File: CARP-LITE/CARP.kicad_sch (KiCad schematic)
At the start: 105 parts, among them J1 USB_C_Receptacle_USB2.0_14P, J10 PYRO_2, J2 SPI1+3V3, J3 I2C1+3V3, J4 2S XT30, J5 UART+5V+I2C1, J6 PYRO_1, J8 PWM1+6V, J9 PWM2+6V, Q1 Q_NMOS, Q2 Q_NMOS, Q4 Q_NMOS, SW1 SW_Push, SW2 SW_Push, U1 W25Q128JVSIMTR (16MB), U2 W25Q32RVXHJQ (2MB), U3 3V3 LDO, U4 RP2350_60QFN, U5 LSM6DSO, U6 BMP390, U7 5V LDO, U8 6V LDO, Y1 ABM8-272-T3

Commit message: fp changes
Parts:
- removed R23: 100, PCM_Resistor_SMD_AKL:R_0603_1608Metric, symbol Device:R
- added R35: 100, Resistor_SMD:R_0603_1608Metric, symbol Device:R
- R1, R11, R14, R15, R16, R17, R18, R2, R3, R6, R7, R9: footprint PCM_Resistor_SMD_AKL:R_0603_1608Metric -> Resistor_SMD:R_0603_1608Metric
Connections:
- net GPIO21: now also R35.1
- net at C27.2, Q2.G, R25.1: now also R35.2
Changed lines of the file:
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@@
 			)
 		)
-		(property "Footprint" "PCM_Resistor_SMD_AKL:R_0603_1608Metric"
+		(property "Footprint" "Resistor_SMD:R_0603_1608Metric"
 			(at 67.31 269.748 90)
 			(hide yes)
@@
 	)
 	(symbol
+		(lib_id "Device:R")
+		(at 328.93 237.49 90)
+		(unit 1)
+		(body_style 1)
+		(exclude_from_sim no)
+		(in_bom yes)
+		(on_board yes)
+		(in_pos_files yes)
+		(dnp no)
+		(property "Reference" "R35"
+			(at 326.644 235.204 90)
+			(show_name no)
+			(do_not_autoplace no)
+			(effects
+				(font
+					(size 1.27 1.27)
+				)
+				(justify right)
+			)
+		)
+		(property "Value" "100"
+			(at 326.898 237.49 90)
+			(show_name no)
+			(do_not_autoplace no)
+			(effects
+				(font
+					(size 1.27 1.27)
+				)
+				(justify right)
+			)
+		)
+		(property "Footprint" "Resistor_SMD:R_0603_1608Metric"
+			(at 328.93 239.268 90)
+			(hide yes)
+			(show_name no)
+			(do_not_autoplace no)
+			(effects
+				(font
+					(size 1.27 1.27)
+				)
+			)
+		)
+		(property "Datasheet" ""
+			(at 328.93 237.49 0)
+			(hide yes)
+			(show_name no)
+			(do_not_autoplace no)
+			(effects
+				(font
+					(size 1.27 1.27)
+				)
+			)
+		)
+		(property "Description" ""
+			(at 328.93 237.49 0)
+			(show_name no)
+			(do_not_autoplace no)
+			(effects
+				(font
+					(size 1.27 1.27)
+				)
+			)
+		)
+		(pin "1"
+		)
+		(pin "2"
+		)
+		(instances
+			(project "CARP"
+				(path "/94683f5c-9cd9-448e-be96-9792537b5cb8"
+					(reference "R35")
+					(unit 1)
+				)
+			)
+		)
+	)
+	(symbol
 		(lib_id "power:GND")
 		(at 351.79 194.31 0)
@@
 			)
 		)
-		(property "Footprint" "PCM_Resistor_SMD_AKL:R_0603_1608Metric"
+		(property "Footprint" "Resistor_SMD:R_0603_1608Metric"
 			(at 240.03 125.222 90)
 			(hide yes)
@@
 			)
 		)
-		(property "Footprint" "PCM_Resistor_SMD_AKL:R_0603_1608Metric"
+		(property "Footprint" "Resistor_SMD:R_0603_1608Metric"
 			(at 250.825 83.312 90)
 			(hide yes)
@@
 	)
 	(symbol
-		(lib_id "Device:R")
-		(at 328.93 237.49 90)
-		(unit 1)
-		(body_style 1)
-		(exclude_from_sim no)
-		(in_bom yes)
-		(on_board yes)
-		(in_pos_files yes)
-		(dnp no)
-		(property "Reference" "R23"
-			(at 326.644 235.204 90)
-			(show_name no)
-			(do_not_autoplace no)
-			(effects
-				(font
-					(size 1.27 1.27)
-				)
-				(justify right)
-			)
-		)
-		(property "Value" "100"
-			(at 326.898 237.49 90)
-			(show_name no)
-			(do_not_autoplace no)
-			(effects
-				(font
-					(size 1.27 1.27)
-				)
-				(justify right)
-			)
-		)
-		(property "Footprint" "PCM_Resistor_SMD_AKL:R_0603_1608Metric"
-			(at 328.93 239.268 90)
-			(hide yes)
-			(show_name no)
-			(do_not_autoplace no)
-			(effects
-				(font
-					(size 1.27 1.27)
-				)
-			)
-		)
-		(property "Datasheet" ""
-			(at 328.93 237.49 0)
-			(hide yes)
-			(show_name no)
-			(do_not_autoplace no)
-			(effects
-				(font
-					(size 1.27 1.27)
-				)
-			)
-		)
-		(property "Description" ""
-			(at 328.93 237.49 0)
-			(show_name no)
-			(do_not_autoplace no)
-			(effects
-				(font
-					(size 1.27 1.27)
-				)
-			)
-		)
-		(pin "1"
-		)
-		(pin "2"
-		)
-		(instances
-			(project "CARP"
-				(path "/94683f5c-9cd9-448e-be96-9792537b5cb8"
-					(reference "R23")
-					(unit 1)
-				)
-			)
-		)
-	)
-	(symbol
 		(lib_id "Device:C")
 		(at 214.63 69.85 0)
@@
 			)
 		)
-		(property "Footprint" "PCM_Resistor_SMD_AKL:R_0603_1608Metric"
+		(property "Footprint" "Resistor_SMD:R_0603_1608Metric"
 			(at 69.342 91.44 90)
 			(hide yes)
@@
 			)
 		)
-		(property "Footprint" "PCM_Resistor_SMD_AKL:R_0603_1608Metric"
+		(property "Footprint" "Resistor_SMD:R_0603_1608Metric"
 			(at 137.922 151.13 90)
 			(hide yes)
@@
 			)
 		)
-		(property "Footprint" "PCM_Resistor_SMD_AKL:R_0603_1608Metric"
+		(property "Footprint" "Resistor_SMD:R_0603_1608Metric"
 			(at 105.918 96.52 90)
 			(hide yes)
@@
 			)
 		)
-		(property "Footprint" "PCM_Resistor_SMD_AKL:R_0603_1608Metric"
+		(property "Footprint" "Resistor_SMD:R_0603_1608Metric"
 			(at 121.92 168.148 90)
 			(hide yes)
@@
 			)
 		)
-		(property "Footprint" "PCM_Resistor_SMD_AKL:R_0603_1608Metric"
+		(property "Footprint" "Resistor_SMD:R_0603_1608Metric"
 			(at 70.612 273.05 90)
 			(hide yes)
@@
 			)
 		)
-		(property "Footprint" "PCM_Resistor_SMD_AKL:R_0603_1608Metric"
+		(property "Footprint" "Resistor_SMD:R_0603_1608Metric"
 			(at 105.918 106.68 90)
 			(hide yes)
@@
 			)
 		)
-		(property "Footprint" "PCM_Resistor_SMD_AKL:R_0603_1608Metric"
+		(property "Footprint" "Resistor_SMD:R_0603_1608Metric"
 			(at 31.75 168.148 90)
 			(hide yes)
@@
 			)
 		)
-		(property "Footprint" "PCM_Resistor_SMD_AKL:R_0603_1608Metric"
+		(property "Footprint" "Resistor_SMD:R_0603_1608Metric"
 			(at 31.75 159.258 90)
 			(hide yes)
@@
 			)
 		)
-		(property "Footprint" "PCM_Resistor_SMD_AKL:R_0603_1608Metric"
+		(property "Footprint" "Resistor_SMD:R_0603_1608Metric"
 			(at 50.292 151.13 90)
 			(hide yes)

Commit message: more fp changes
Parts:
- removed Q1, Q2, Q4: Q_NMOS, symbol Device:Q_NMOS
- added Q5, Q6, Q7: SQ2318CES, Package_TO_SOT_SMD:SOT-23, symbol Transistor_FET_Other:Q_NMOS_Depletion_GSD
- D2: footprint (none) -> LED_SMD:LED_0805_2012Metric
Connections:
- net GND: now also Q5.2 (S), Q6.2 (S), Q7.2 (S)
- net at R14.1, R15.2: now also Q7.1 (G)
- net at C27.2, R25.1, R35.2: now also Q5.1 (G)
- net at J10.2 (Pin_2), R32.2: now also Q6.3 (D)
- net at C33.2, R31.2, R33.1: now also Q6.1 (G)
- net at J6.2 (Pin_2), R24.2: now also Q5.3 (D)
- net at BZ1.2 (-), D5.2 (A): now also Q7.3 (D)

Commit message: siup
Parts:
- BZ1: footprint (none) -> Buzzer_Beeper:Buzzer_12x9.5RM7.6
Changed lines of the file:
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@@
 			)
 		)
-		(property "Footprint" ""
+		(property "Footprint" "Buzzer_Beeper:Buzzer_12x9.5RM7.6"
 			(at 70.485 254 90)
 			(hide yes)

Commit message: change jst to picoblade
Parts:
- J2, J5: footprint Connector_JST:JST_SH_BM06B-SRSS-TB_1x06-1MP_P1.00mm_Vertical -> Connector_Molex:Molex_PicoBlade_53047-0610_1x06_P1.25mm_Vertical
- J3: footprint Connector_JST:JST_SH_BM04B-SRSS-TB_1x04-1MP_P1.00mm_Vertical -> Connector_Molex:Molex_PicoBlade_53047-0410_1x04_P1.25mm_Vertical
- J8, J9: footprint Connector_JST:JST_SH_BM03B-SRSS-TB_1x03-1MP_P1.00mm_Vertical -> Connector_Molex:Molex_PicoBlade_53047-0310_1x03_P1.25mm_Vertical
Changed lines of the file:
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@@
 			)
 		)
-		(property "Footprint" "Connector_JST:JST_SH_BM06B-SRSS-TB_1x06-1MP_P1.00mm_Vertical"
+		(property "Footprint" "Connector_Molex:Molex_PicoBlade_53047-0610_1x06_P1.25mm_Vertical"
 			(at 217.17 189.23 0)
 			(hide yes)
@@
 			)
 		)
-		(property "Footprint" "Connector_JST:JST_SH_BM04B-SRSS-TB_1x04-1MP_P1.00mm_Vertical"
+		(property "Footprint" "Connector_Molex:Molex_PicoBlade_53047-0410_1x04_P1.25mm_Vertical"
 			(at 217.17 210.82 0)
 			(hide yes)
@@
 			)
 		)
-		(property "Footprint" "Connector_JST:JST_SH_BM03B-SRSS-TB_1x03-1MP_P1.00mm_Vertical"
+		(property "Footprint" "Connector_Molex:Molex_PicoBlade_53047-0310_1x03_P1.25mm_Vertical"
 			(at 217.17 254 0)
 			(hide yes)
@@
 			)
 		)
-		(property "Footprint" "Connector_JST:JST_SH_BM03B-SRSS-TB_1x03-1MP_P1.00mm_Vertical"
+		(property "Footprint" "Connector_Molex:Molex_PicoBlade_53047-0310_1x03_P1.25mm_Vertical"
 			(at 217.17 270.51 0)
 			(hide yes)
@@
 			)
 		)
-		(property "Footprint" "Connector_JST:JST_SH_BM06B-SRSS-TB_1x06-1MP_P1.00mm_Vertical"
+		(property "Footprint" "Connector_Molex:Molex_PicoBlade_53047-0610_1x06_P1.25mm_Vertical"
 			(at 217.17 233.68 0)
 			(hide yes)

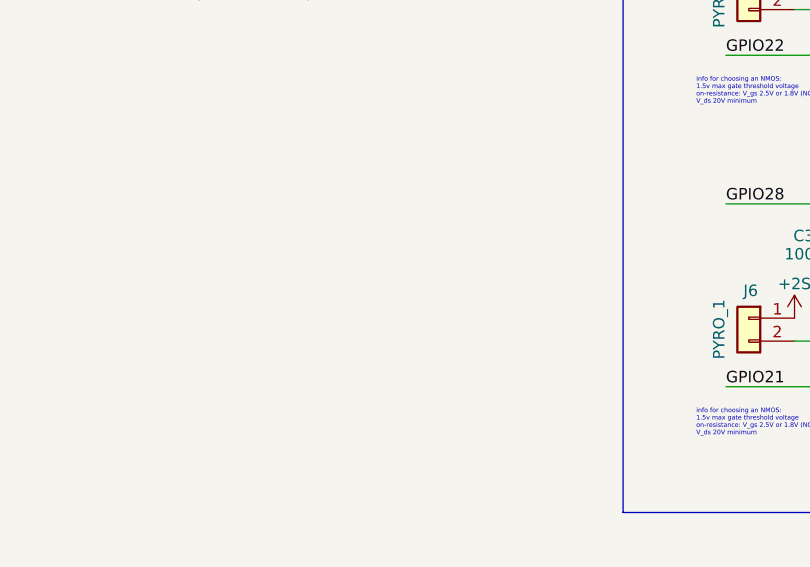
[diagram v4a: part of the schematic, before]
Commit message: Add LR2021 symbol
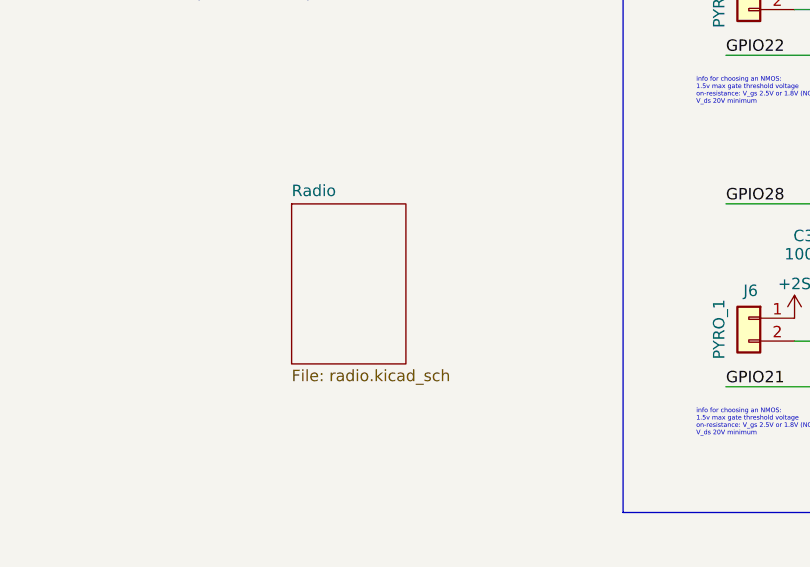
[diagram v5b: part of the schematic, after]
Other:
- added sheet Radio (radio.kicad_sch)
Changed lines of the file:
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@@
+		)
+	)
+	(sheet
+		(at 262.89 217.17)
+		(size 12.7 17.78)
+		(exclude_from_sim no)
+		(in_bom yes)
+		(on_board yes)
+		(dnp no)
+		(fields_autoplaced yes)
+		(stroke
+			(width 0.1524)
+			(type solid)
+		)
+		(fill
+			(color 0 0 0 0)
+		)
+		(property "Sheetname" "Radio"
+			(at 262.89 216.4584 0)
+			(show_name no)
+			(do_not_autoplace no)
+			(effects
+				(font
+					(size 1.27 1.27)
+				)
+				(justify left bottom)
+			)
+		)
+		(property "Sheetfile" "radio.kicad_sch"
+			(at 262.89 235.5346 0)
+			(show_name no)
+			(do_not_autoplace no)
+			(effects
+				(font
+					(size 1.27 1.27)
+				)
+				(justify left top)
+			)
+		)
+		(instances
+			(project "CARP"
+				(path "/94683f5c-9cd9-448e-be96-9792537b5cb8"
+					(page "2")
+				)
+			)
 		)
 	)

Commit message: radio idk
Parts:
- removed J2: SPI1+3V3, Connector_Molex:Molex_PicoBlade_53047-0610_1x06_P1.25mm_Vertical, symbol Connector_Generic:Conn_01x06
- J1: value USB_C_Receptacle_USB2.0_14P -> USB-C; symbol Connector:USB_C_Receptacle_USB2.0_14P -> Connector:USB_C_Receptacle_USB2.0_16P
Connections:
- net GND: now also J1.SH (SHIELD); no longer J1.S1 (SHIELD)
- no-connect marks 1 -> 8
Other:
- sheet Radio ports: added RADIO_BUSY, RADIO_CS, RADIO_DIO5, RADIO_DIO6, RADIO_MISO, RADIO_MOSI, RADIO_SCK, ~{RADIO_RESET}; removed none
- note added: "Mounting"
- note added: "Radio"
- note added: "Replace with buck converter? idk how much current servos take"
- moved on the sheet: H1, H2, H3, H4

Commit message: Update button footprint to proper one
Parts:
- SW1, SW2: footprint Button_Switch_SMD:SW_Push_1P1T_NO_Vertical_Wuerth_434133025816 -> Button_Switch_SMD:SW_Push_1P1T_XKB_TS-1187A
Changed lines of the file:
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@@
 			)
 		)
-		(property "Footprint" "Button_Switch_SMD:SW_Push_1P1T_NO_Vertical_Wuerth_434133025816"
+		(property "Footprint" "Button_Switch_SMD:SW_Push_1P1T_XKB_TS-1187A"
 			(at 250.19 121.92 0)
 			(hide yes)
@@
 			)
 		)
-		(property "Footprint" "Button_Switch_SMD:SW_Push_1P1T_NO_Vertical_Wuerth_434133025816"
+		(property "Footprint" "Button_Switch_SMD:SW_Push_1P1T_XKB_TS-1187A"
 			(at 229.235 92.71 0)
 			(hide yes)

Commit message: do pyro shebang and pcb work
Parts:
- removed JP1: SolderJumper_3_Bridged12, Jumper:SolderJumper-3_P1.3mm_Bridged12_RoundedPad1.0x1.5mm_NumberLabels, symbol Jumper:SolderJumper_3_Bridged12
- R24, R25, R26, R31, R32, R33, R34, R35: footprint Resistor_SMD:R_0603_1608Metric -> Resistor_SMD:R_0402_1005Metric
- R27, R28, R29, R30: footprint Resistor_SMD:R_0402_1005Metric_Pad0.72x0.64mm_HandSolder -> Jumper:SolderJumper-2_P1.3mm_Bridged_RoundedPad1.0x1.5mm
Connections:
- net GND: now also U6.5 (SDO)
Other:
- note added: "##### TODO ##### choose and optimize footprints: - main cap (move from servo out to 2S ?) - buzzer ponder servo power keep slaving away at the pcb"
- note added: "Default address: 0x76"
- note removed: "##### TODO ##### choose and optimize footprints double check pyro circuits ponder servo power"
- note removed: "Default address: 0x76 Alternative address: 0x77"
